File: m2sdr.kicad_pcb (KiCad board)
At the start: 2 copper layers, 30 x 38 mm, 2 parts, among them J1 Bus_M.2_Socket_B

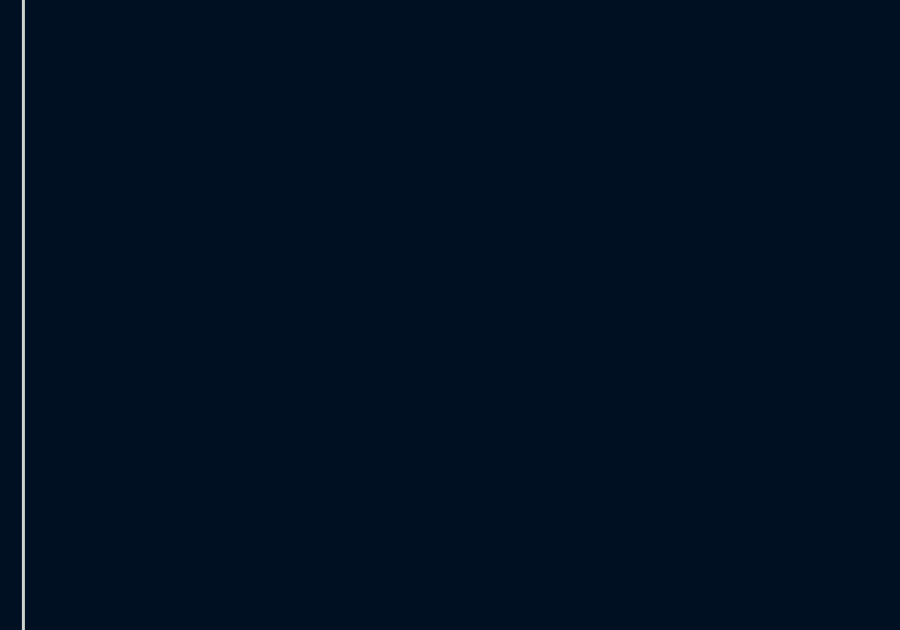
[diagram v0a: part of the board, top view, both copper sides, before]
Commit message: add footprint for testing
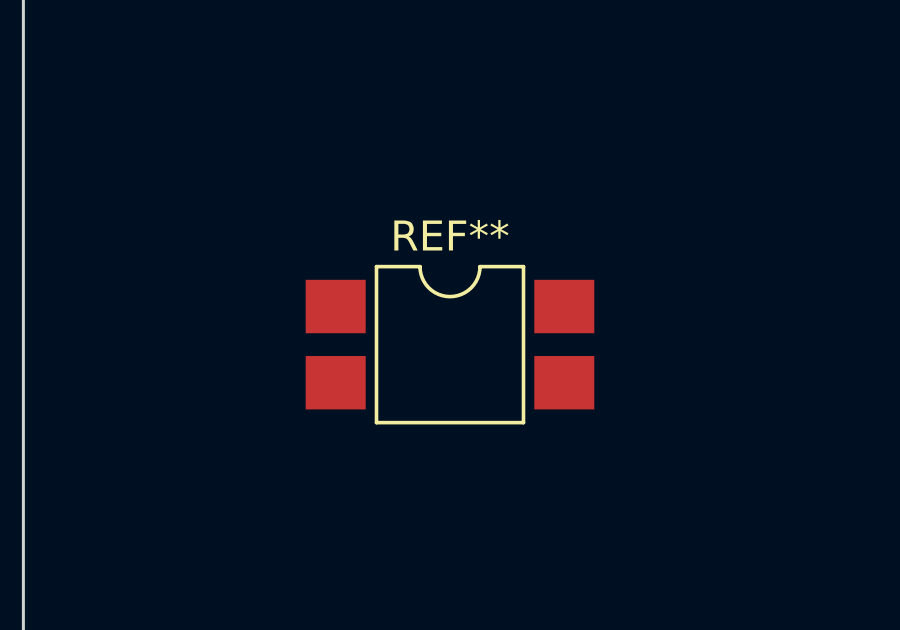
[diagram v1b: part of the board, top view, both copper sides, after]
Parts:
- added REF**: SMDIP-4_W7.62mm, Package_DIP:SMDIP-4_W7.62mm, F.Cu at (109.2, 116.8)
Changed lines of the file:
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@@
       (net 53 "unconnected-(J1-CONFIG_2-Pad75)") (pinfunction "CONFIG_2") (pintype "input"))
+  )
+  (footprint "Package_DIP:SMDIP-4_W7.62mm" (layer "F.Cu")
+    (at 109.22 116.84)
+    (descr "4-lead surface-mounted (SMD) DIP package, row spacing 7.62 mm (300 mils)")
+    (tags "SMD DIP DIL PDIP SMDIP 2.54mm 7.62mm 300mil")
+    (attr smd)
+    (fp_text reference "REF**" (at 0 -3.6) (layer "F.SilkS")
+        (effects (font (size 1 1) (thickness 0.15)))
+    )
+    (fp_text value "SMDIP-4_W7.62mm" (at 0 3.6) (layer "F.Fab")
+        (effects (font (size 1 1) (thickness 0.15)))
+    )
+    (fp_text user "${REFERENCE}" (at 0 0) (layer "F.Fab")
+        (effects (font (size 1 1) (thickness 0.15)))
+    )
+    (fp_line (start -2.45 -2.6) (end -2.45 2.6)
+      (stroke (width 0.12) (type solid)) (layer "F.SilkS"))
+    (fp_line (start -2.45 2.6) (end 2.45 2.6)
+      (stroke (width 0.12) (type solid)) (layer "F.SilkS"))
+    (fp_line (start -1 -2.6) (end -2.45 -2.6)
+      (stroke (width 0.12) (type solid)) (layer "F.SilkS"))
+    (fp_line (start 2.45 -2.6) (end 1 -2.6)
+      (stroke (width 0.12) (type solid)) (layer "F.SilkS"))
+    (fp_line (start 2.45 2.6) (end 2.45 -2.6)
+      (stroke (width 0.12) (type solid)) (layer "F.SilkS"))
+    (fp_arc (start 1 -2.6) (mid 0 -1.6) (end -1 -2.6)
+      (stroke (width 0.12) (type solid)) (layer "F.SilkS"))
+    (fp_line (start -5.1 -2.8) (end -5.1 2.8)
+      (stroke (width 0.05) (type solid)) (layer "F.CrtYd"))
+    (fp_line (start -5.1 2.8) (end 5.1 2.8)
+      (stroke (width 0.05) (type solid)) (layer "F.CrtYd"))
+    (fp_line (start 5.1 -2.8) (end -5.1 -2.8)
+      (stroke (width 0.05) (type solid)) (layer "F.CrtYd"))
+    (fp_line (start 5.1 2.8) (end 5.1 -2.8)
+      (stroke (width 0.05) (type solid)) (layer "F.CrtYd"))
+    (fp_line (start -3.175 -1.54) (end -2.175 -2.54)
+      (stroke (width 0.1) (type solid)) (layer "F.Fab"))
+    (fp_line (start -3.175 2.54) (end -3.175 -1.54)
+      (stroke (width 0.1) (type solid)) (layer "F.Fab"))
+    (fp_line (start -2.175 -2.54) (end 3.175 -2.54)
+      (stroke (width 0.1) (type solid)) (layer "F.Fab"))
+    (fp_line (start 3.175 -2.54) (end 3.175 2.54)
+      (stroke (width 0.1) (type solid)) (layer "F.Fab"))
+    (fp_line (start 3.175 2.54) (end -3.175 2.54)
+      (stroke (width 0.1) (type solid)) (layer "F.Fab"))
+    (pad "1" smd rect (at -3.81 -1.27) (size 2 1.78) (layers "F.Cu" "F.Paste" "F.Mask"))
+    (pad "2" smd rect (at -3.81 1.27) (size 2 1.78) (layers "F.Cu" "F.Paste" "F.Mask"))
+    (pad "3" smd rect (at 3.81 1.27) (size 2 1.78) (layers "F.Cu" "F.Paste" "F.Mask"))
+    (pad "4" smd rect (at 3.81 -1.27) (size 2 1.78) (layers "F.Cu" "F.Paste" "F.Mask"))
+    (model "${KICAD6_3DMODEL_DIR}/Package_DIP.3dshapes/SMDIP-4_W7.62mm.wrl"
+      (offset (xyz 0 0 0))
+      (scale (xyz 1 1 1))
+      (rotate (xyz 0 0 0))
+    )
   )
   (footprint "TestPoint:TestPoint_Plated_Hole_D3.0mm" (layer "F.Cu")
